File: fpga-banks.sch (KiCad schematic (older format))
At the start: 3 parts, among them U1 XC7K70T-FBG484, U2 ASEM1-100.000MHZ-LC-T

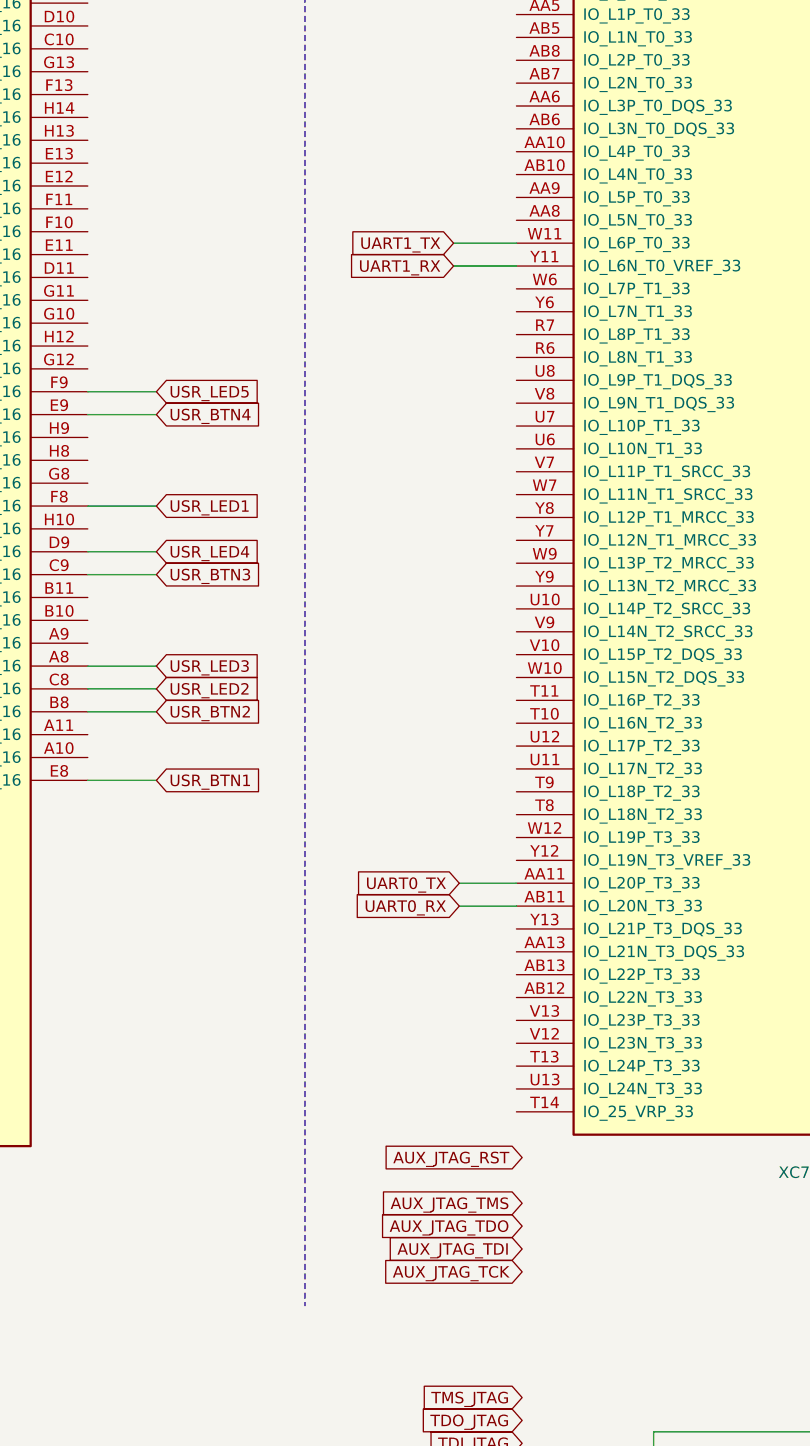
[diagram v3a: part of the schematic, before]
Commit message: Connect remaining AUX JTAG signals
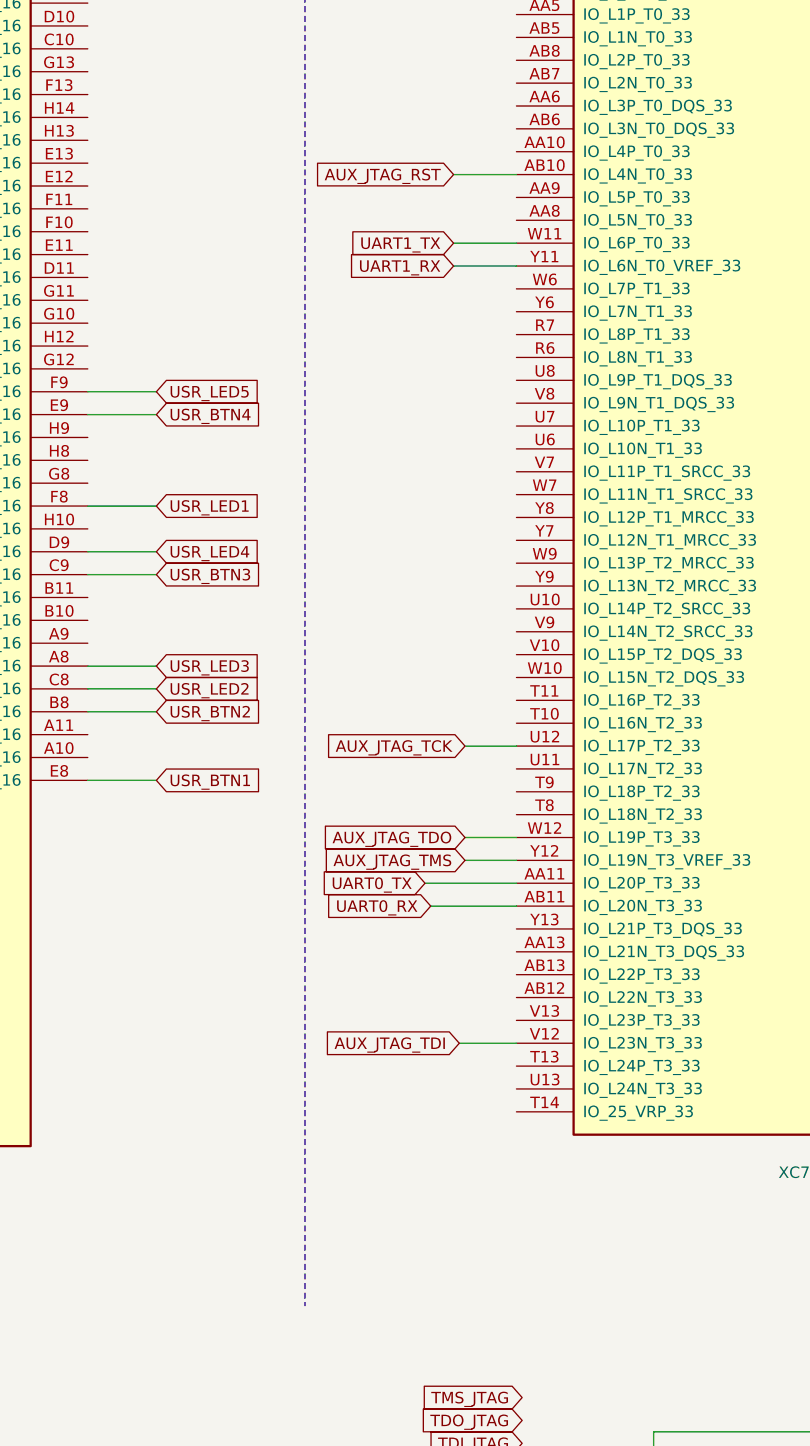
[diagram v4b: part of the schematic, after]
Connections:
- net AUX_JTAG_RST: now also U1.AB10 (IO_L4N_T0_33)
- net AUX_JTAG_TCK: now also U1.U12 (IO_L17P_T2_33)
- net AUX_JTAG_TDI: now also U1.V12 (IO_L23N_T3_33)
- net AUX_JTAG_TDO: now also U1.W12 (IO_L19P_T3_33)
- net AUX_JTAG_TMS: now also U1.Y12 (IO_L19N_T3_VREF_33)
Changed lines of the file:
@@
 Text GLabel 12125 8375 0    50   Input ~ 0
 TMS_JTAG
-Text GLabel 12125 7725 0    50   Input ~ 0
+Text GLabel 11850 6825 0    50   Input ~ 0
 AUX_JTAG_TDI
-Text GLabel 12125 7625 0    50   Input ~ 0
+Text GLabel 11875 5925 0    50   Input ~ 0
 AUX_JTAG_TDO
-Text GLabel 12125 7525 0    50   Input ~ 0
+Text GLabel 11875 6025 0    50   Input ~ 0
 AUX_JTAG_TMS
-Text GLabel 11850 6225 0    50   Input ~ 0
+Text GLabel 11725 6225 0    50   Input ~ 0
 UART0_RX
 Text GLabel 11825 3425 0    50   Input ~ 0
 UART1_RX
-Text GLabel 11850 6125 0    50   Input ~ 0
+Text GLabel 11700 6125 0    50   Input ~ 0
 UART0_TX
 Text GLabel 11825 3325 0    50   Input ~ 0
 UART1_TX
-Text GLabel 12125 7825 0    50   Input ~ 0
+Text GLabel 11875 5525 0    50   Input ~ 0
 AUX_JTAG_TCK
-Text GLabel 12125 7325 0    50   Input ~ 0
+Text GLabel 11825 3025 0    50   Input ~ 0
 AUX_JTAG_RST
 Wire Wire Line
-	12100 6225 11850 6225
+	12100 6225 11725 6225
 Wire Wire Line
-	12100 6125 11850 6125
+	12100 6125 11700 6125
 Wire Wire Line
 	12100 3325 11825 3325
 Wire Wire Line
 	12100 3425 11825 3425
+Wire Wire Line
+	11875 6025 12100 6025
+Wire Wire Line
+	12100 5925 11875 5925
+Wire Wire Line
+	11850 6825 12100 6825
+Wire Wire Line
+	11875 5525 12100 5525
+Wire Wire Line
+	12100 3025 11825 3025
 $EndSCHEMATC

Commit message: Connected RGMII - Wip
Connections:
- net ETH_MDC: now also U1.C14 (IO_L7P_T1_AD10P_15)
- net ETH_MDIO: now also U1.C12 (IO_L2P_T0_AD8P_15)
- net ETH_REF_CLK: now also U1.C15 (IO_L7N_T1_AD10N_15)
- net ETH_TX_RSTN: now also U1.C13 (IO_L5P_T0_AD2P_15)
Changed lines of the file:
@@
 	8400 1350 8400 1250
 Connection ~ 8225 1350
-Text GLabel 8125 7800 0    50   Input ~ 0
-ETH_REF_CLK
 Text GLabel 6925 4075 0    50   Input ~ 0
 ETH_RXD0
@@
 Text GLabel 6975 3075 0    50   Input ~ 0
 ETH_RXERR
-Text GLabel 8125 7550 0    50   Input ~ 0
+Text GLabel 6975 3175 0    50   Input ~ 0
 ETH_TX_RSTN
 Text GLabel 6925 4275 0    50   Input ~ 0
@@
 Text GLabel 6950 6575 0    50   Input ~ 0
 ETH_TXD2
-Text GLabel 8000 7425 0    50   Input ~ 0
+Text GLabel 6950 2575 0    50   Input ~ 0
 ETH_MDIO
 Text GLabel 6975 3975 0    50   Input ~ 0
@@
 Text GLabel 6950 3775 0    50   Input ~ 0
 ETH_RXD1
-Text GLabel 6925 2975 0    50   Input ~ 0
+Text GLabel 6975 2975 0    50   Input ~ 0
 ETH_CRS
 Text GLabel 7000 6275 0    50   Input ~ 0
 ETH_TXD0
-Text GLabel 7975 7675 0    50   Input ~ 0
+Text GLabel 6950 3575 0    50   Input ~ 0
 ETH_MDC
 Text GLabel 6950 2675 0    50   Input ~ 0
@@
 	6975 3275 7325 3275
 Wire Wire Line
-	6925 2975 7325 2975
+	6975 2975 7325 2975
 Wire Wire Line
 	6925 4075 7325 4075
@@
 Wire Wire Line
 	12100 3025 11825 3025
+Wire Wire Line
+	7325 2575 6950 2575
+Wire Wire Line
+	7325 3175 6975 3175
+Wire Wire Line
+	7325 3575 6950 3575
+Wire Wire Line
+	7325 3675 6950 3675
+Text GLabel 6950 3675 0    50   Input ~ 0
+ETH_REF_CLK
 $EndSCHEMATC

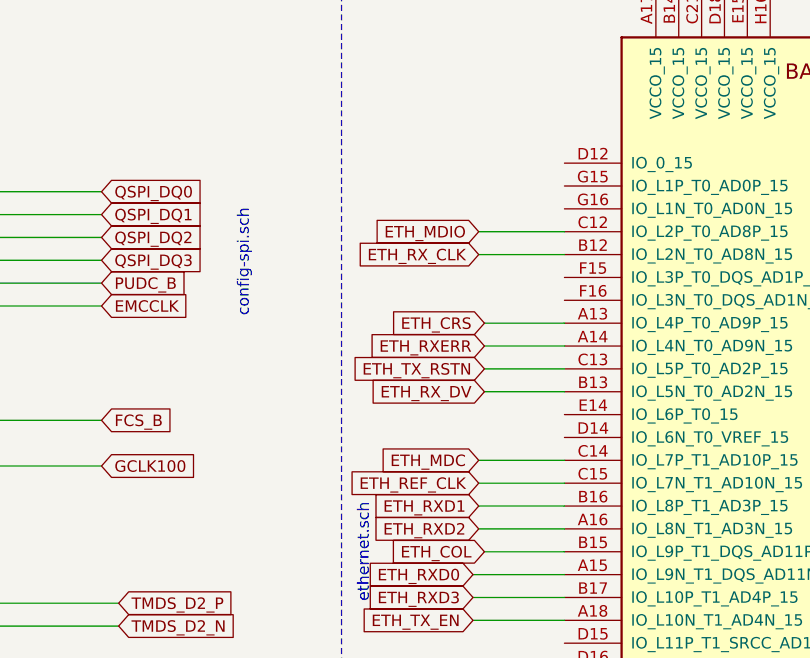
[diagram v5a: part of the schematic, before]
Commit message: Change RGMII control signal assignment
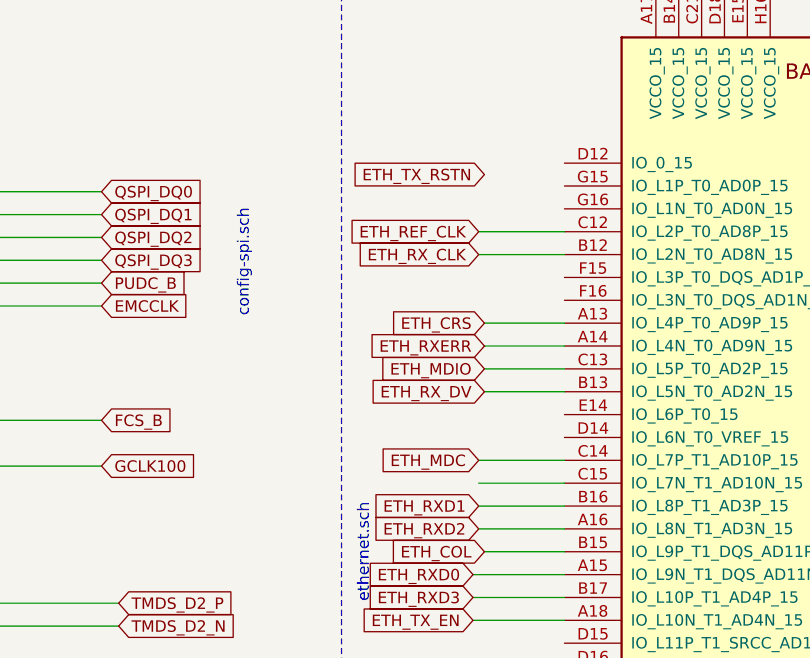
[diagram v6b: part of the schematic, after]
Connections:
- net ETH_MDIO: now also U1.C13 (IO_L5P_T0_AD2P_15); no longer U1.C12 (IO_L2P_T0_AD8P_15)
- net ETH_REF_CLK: now also U1.C12 (IO_L2P_T0_AD8P_15); no longer U1.C15 (IO_L7N_T1_AD10N_15)
- net ETH_TX_RSTN: no longer U1.C13 (IO_L5P_T0_AD2P_15)
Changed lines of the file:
@@
 Text GLabel 6975 3075 0    50   Input ~ 0
 ETH_RXERR
-Text GLabel 6975 3175 0    50   Input ~ 0
+Text GLabel 6975 2325 0    50   Input ~ 0
 ETH_TX_RSTN
 Text GLabel 6925 4275 0    50   Input ~ 0
@@
 Text GLabel 6950 6575 0    50   Input ~ 0
 ETH_TXD2
-Text GLabel 6950 2575 0    50   Input ~ 0
+Text GLabel 6975 3175 0    50   Input ~ 0
 ETH_MDIO
 Text GLabel 6975 3975 0    50   Input ~ 0
@@
 Wire Wire Line
 	7325 3675 6950 3675
-Text GLabel 6950 3675 0    50   Input ~ 0
+Text GLabel 6950 2575 0    50   Input ~ 0
 ETH_REF_CLK
 $EndSCHEMATC

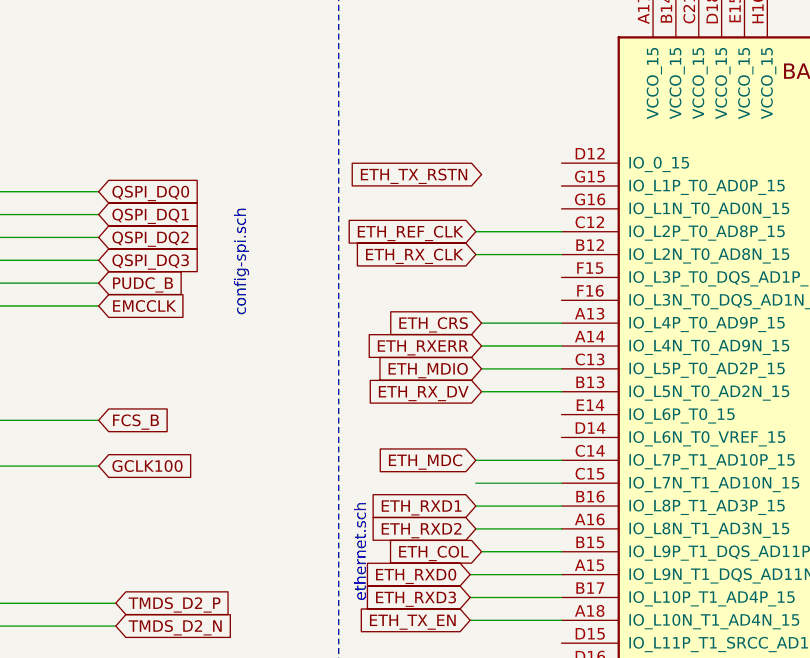
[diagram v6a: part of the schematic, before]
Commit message: Update RGMII connector, started DRAM DQ equalization
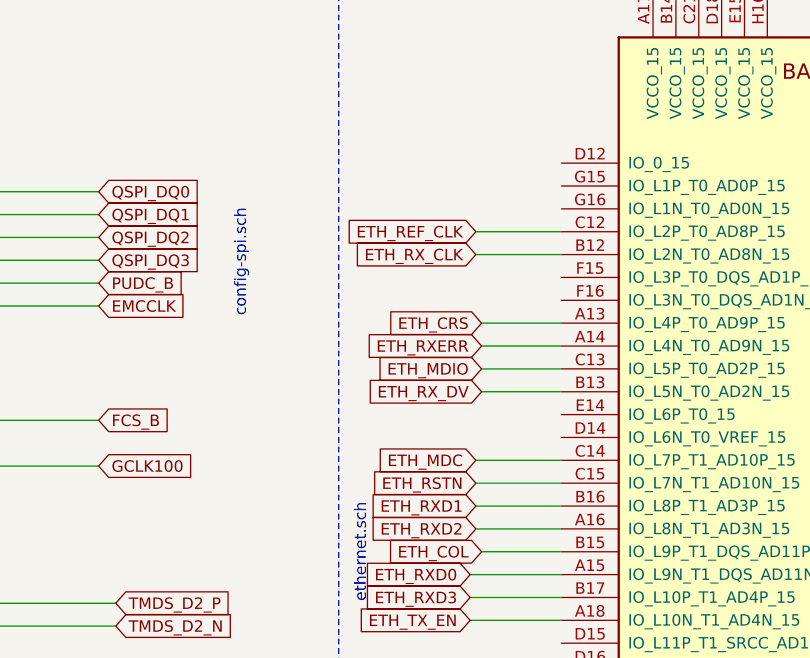
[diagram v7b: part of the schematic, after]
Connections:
- net ETH_RSTN: now reaches U1.C15 (IO_L7N_T1_AD10N_15)
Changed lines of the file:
@@
 Text GLabel 6975 3075 0    50   Input ~ 0
 ETH_RXERR
-Text GLabel 6975 2325 0    50   Input ~ 0
-ETH_TX_RSTN
+Text GLabel 6950 3675 0    50   Input ~ 0
+ETH_RSTN
 Text GLabel 6925 4275 0    50   Input ~ 0
 ETH_TX_EN

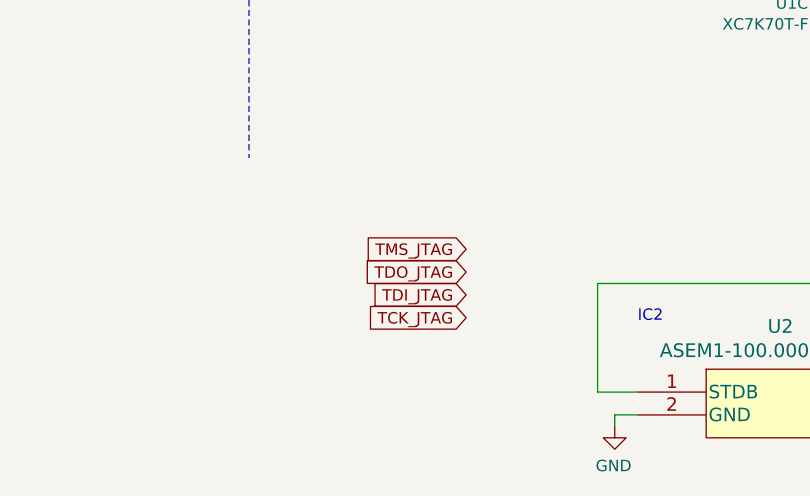
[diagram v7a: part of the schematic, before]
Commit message: Clean up schematic
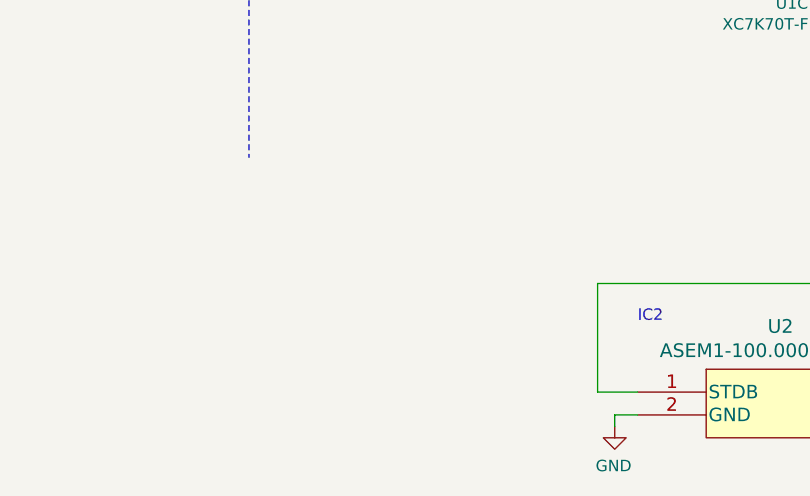
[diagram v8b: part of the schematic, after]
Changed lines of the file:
@@
 $EndComp
 NoConn ~ 1900 2800
-Text GLabel 12125 8675 0    50   Input ~ 0
-TCK_JTAG
-Text GLabel 12125 8575 0    50   Input ~ 0
-TDI_JTAG
-Text GLabel 12125 8475 0    50   Input ~ 0
-TDO_JTAG
-Text GLabel 12125 8375 0    50   Input ~ 0
-TMS_JTAG
 Text GLabel 11850 6825 0    50   Input ~ 0
 AUX_JTAG_TDI
